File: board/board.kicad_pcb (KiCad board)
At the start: 2 copper layers, 21 x 13 mm, 1 part

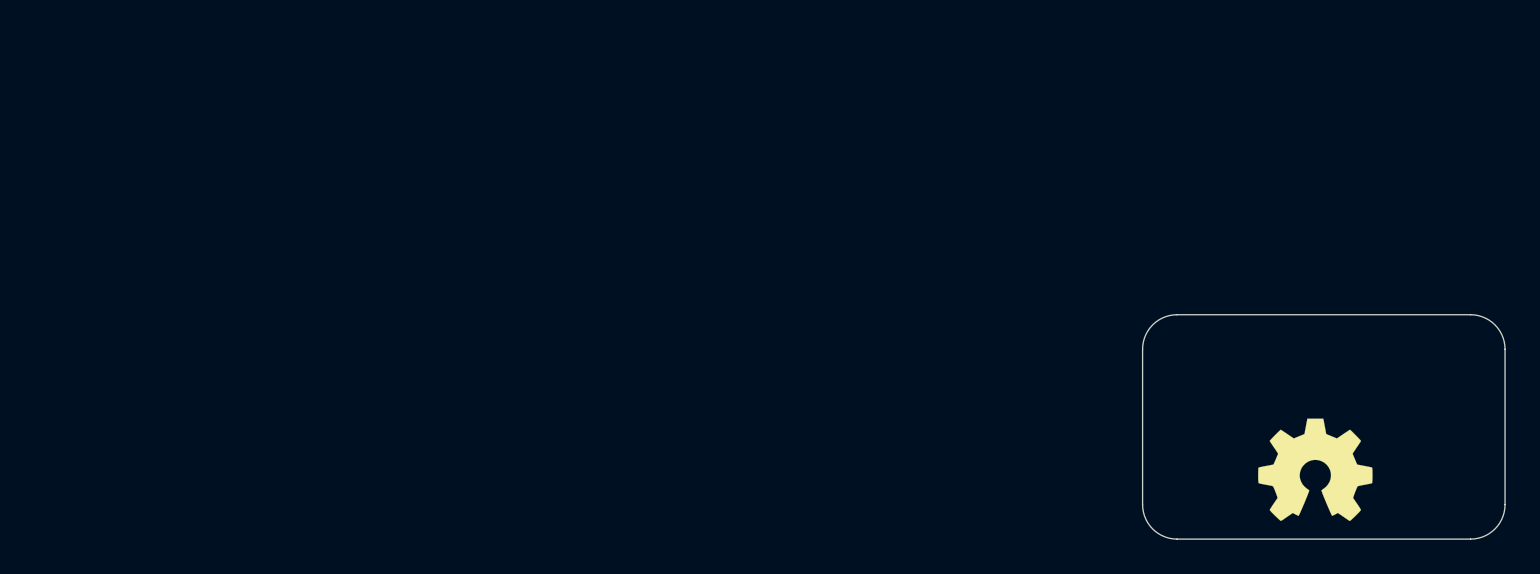
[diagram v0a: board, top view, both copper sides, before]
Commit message: added lcsc numbers and updated to kicad 8
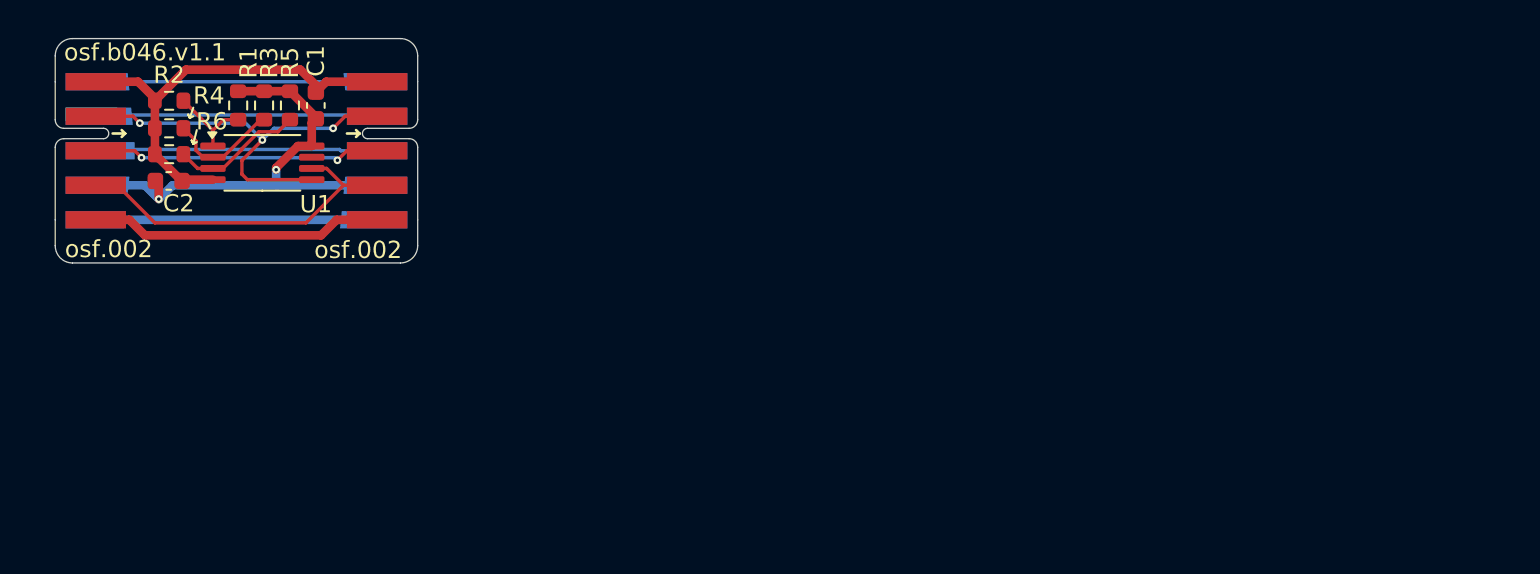
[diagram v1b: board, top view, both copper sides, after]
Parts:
- removed LOGO1: Logo_Open_Hardware_Small, Symbol:OSHW-Symbol_6.7x6mm_SilkScreen
- added C1: 100nF, Capacitor_SMD:C_0603_1608Metric, F.Cu at (92.1, 77.9)
- added C2: 1uF, Capacitor_SMD:C_0603_1608Metric, F.Cu at (83.6, 82.2)
- added J1: 001_I2C, on_edge:on_edge_2x05_device, F.Cu at (77.0, 80.5)
- added J2: 001_I2C, on_edge:on_edge_2x05_host, F.Cu at (98.0, 80.5)
- added R1: 0R, Resistor_SMD:R_0603_1608Metric, F.Cu at (87.6, 77.9)
- added R2: 0R, Resistor_SMD:R_0603_1608Metric, F.Cu at (83.6, 77.6)
- added R3: 0R, Resistor_SMD:R_0603_1608Metric, F.Cu at (89.1, 77.9)
- added R4: 0R, Resistor_SMD:R_0603_1608Metric, F.Cu at (83.6, 79.2)
- added R5: 0R, Resistor_SMD:R_0603_1608Metric, F.Cu at (90.6, 77.9)
- added R6: 0R, Resistor_SMD:R_0603_1608Metric, F.Cu at (83.6, 80.7)
- added U1: M24C02-FDW, Package_SO:TSSOP-8_4.4x3mm_P0.65mm, F.Cu at (89.0, 81.2)
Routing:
- net +3.3V: track 0.00 -> 28.4 mm, vias 0 -> 2
- net GND: track 0.00 -> 25.8 mm
- net /eeprom/SDA: track 0.00 -> 24.1 mm, vias 0 -> 3
- net /eeprom/SCL: track 0.00 -> 20.3 mm
- net Net-(J1-INT): track 0.00 -> 17.0 mm
- net Net-(J1-N/C): track 0.00 -> 16.8 mm, vias 0 -> 2
- net Net-(J1-status): track 0.00 -> 16.6 mm
- net Net-(J1-5V): track 0.00 -> 16.2 mm
- net Net-(J1-CS/EN): track 0.00 -> 16.2 mm
- net Net-(J1-~{RESET}): track 0.00 -> 16.1 mm
- net Net-(U1-E2): track 0.00 -> 7.71 mm
- net Net-(U1-E1): track 0.00 -> 6.59 mm
- net Net-(U1-E0): track 0.00 -> 5.05 mm
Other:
- outline, holes or cut-outs redrawn
- rule pad_to_mask_clearance: 0 -> 0.04
- board text added: "osf.002"
- board text added: "osf.b046.v1.1"
